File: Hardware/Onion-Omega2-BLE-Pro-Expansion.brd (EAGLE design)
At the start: 57 x 39 mm, 50 parts, among them J1 USB-MICROB, J2 USB-A-H, Q1 12Mhz 3225 Package

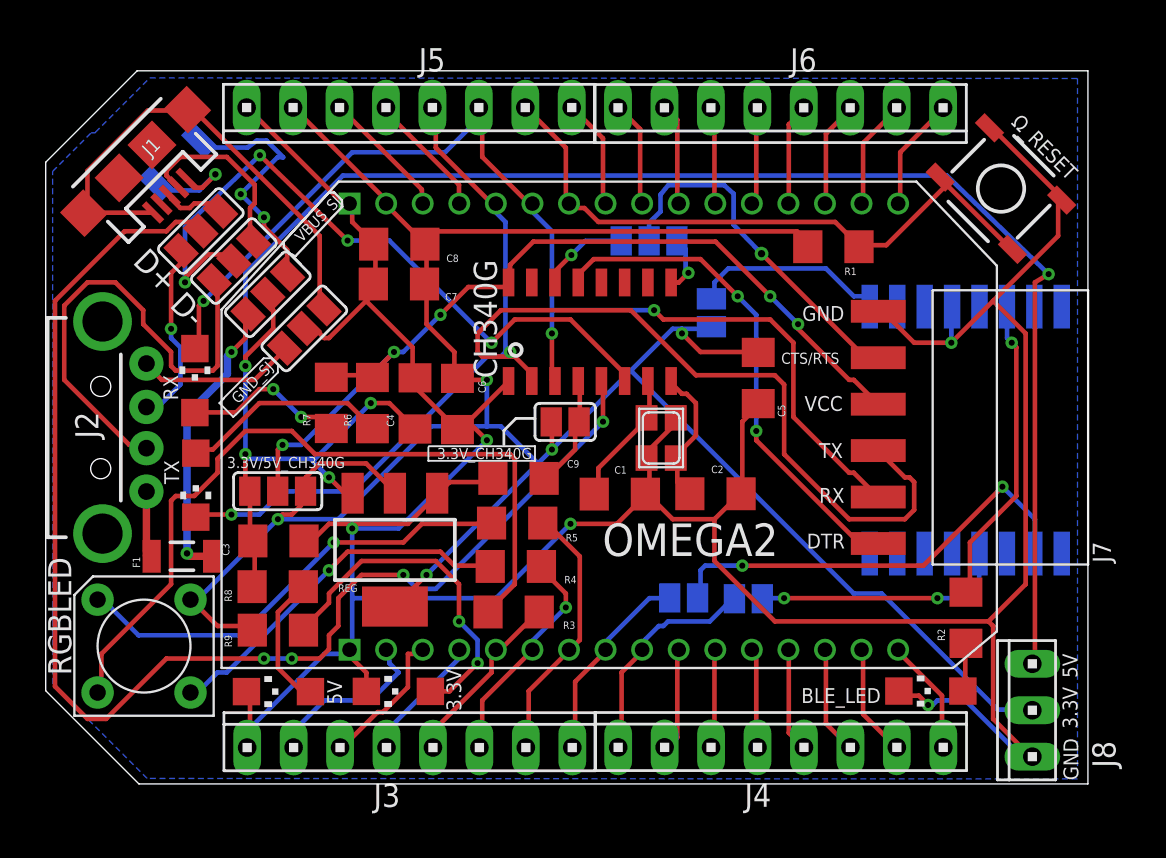
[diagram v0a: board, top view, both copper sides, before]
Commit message: VBUS fused moved after jumper. Resistors for D+ and D- Lines. TODO: Reduce D+ line length
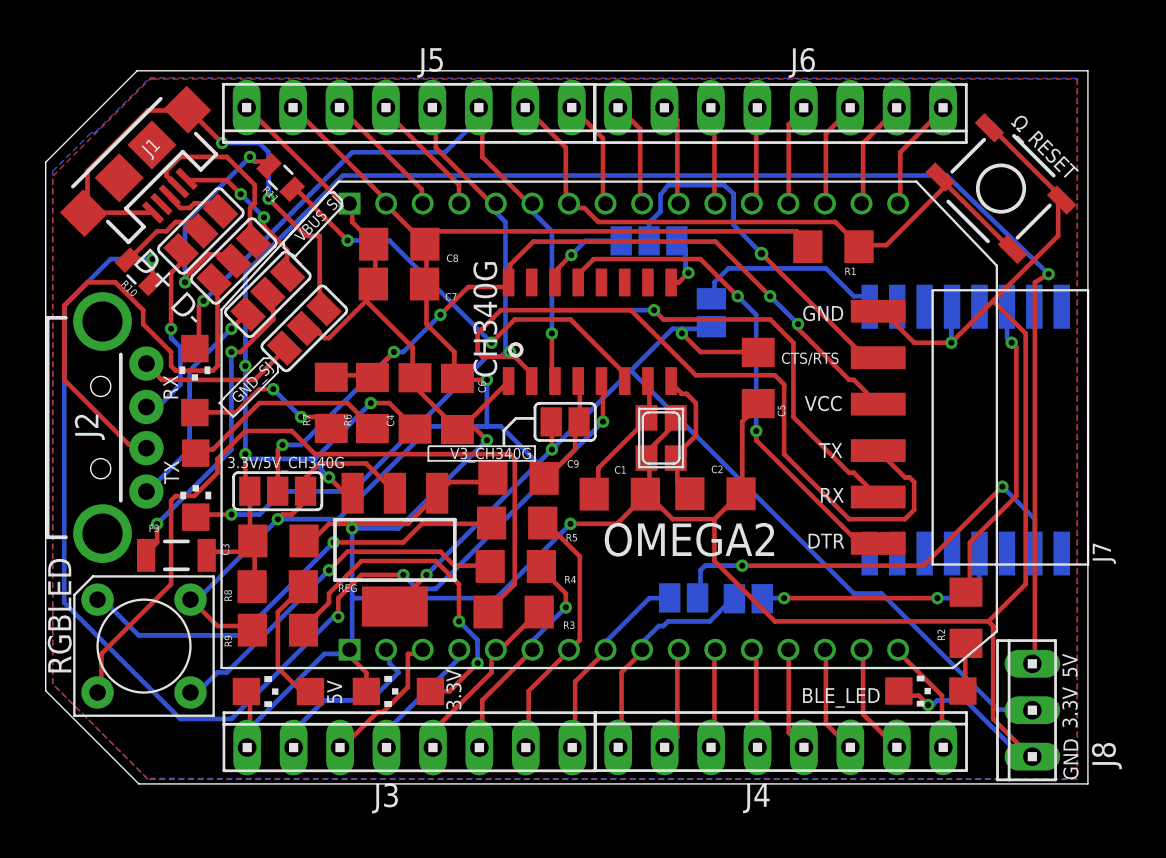
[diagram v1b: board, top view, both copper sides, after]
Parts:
- removed F1, F2: PTCSMD-W, SparkFun-PowerIC:PTC-1206-WIDE
- added F3: PTCSMD-W, SparkFun-PowerIC:PTC-1206-WIDE
- added R10, R11: (no value), SparkFun-Passives:0805
- renumbered 3.3V_CH340G to V3_CH340G
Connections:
- new net N$38: D+.2, R10.2
- net 5V: now also F3.2; no longer VBUS_SJ.2
- net D+: now also R10.1; no longer D+.2
- net D-: now also R11.1; no longer D-.2
- net N$27: now also F3.1, VBUS_SJ.2; no longer F2.1, J1.VBUS
- net N$37: now also VBUS_SJ.1; no longer F1.1
- net N$41: now also J1.VBUS; no longer F2.2
- net N$44: now also D-.2, R11.2; no longer F1.2, VBUS_SJ.1
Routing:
- net D-: track 38.7 -> 23.9 mm, vias 4 -> 2
- net N$27: track 5.83 -> 17.6 mm, vias 1 -> 2
- net N$37: track 3.95 -> 12.1 mm, vias 0 -> 1
- net D+: track 72.8 -> 65.8 mm
- net N$41: track 13.9 -> 8.74 mm
- net N$38: track 0.00 -> 5.12 mm
- net N$44: track 16.0 -> 13.3 mm
- net N$40: track 27.5 -> 28.8 mm, vias 0 -> 2
- net 5V: track 106.6 -> 105.3 mm
- added copper zone on layer 1, net 3.3V

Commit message: CTS and RTS lines seperated. Sent for production
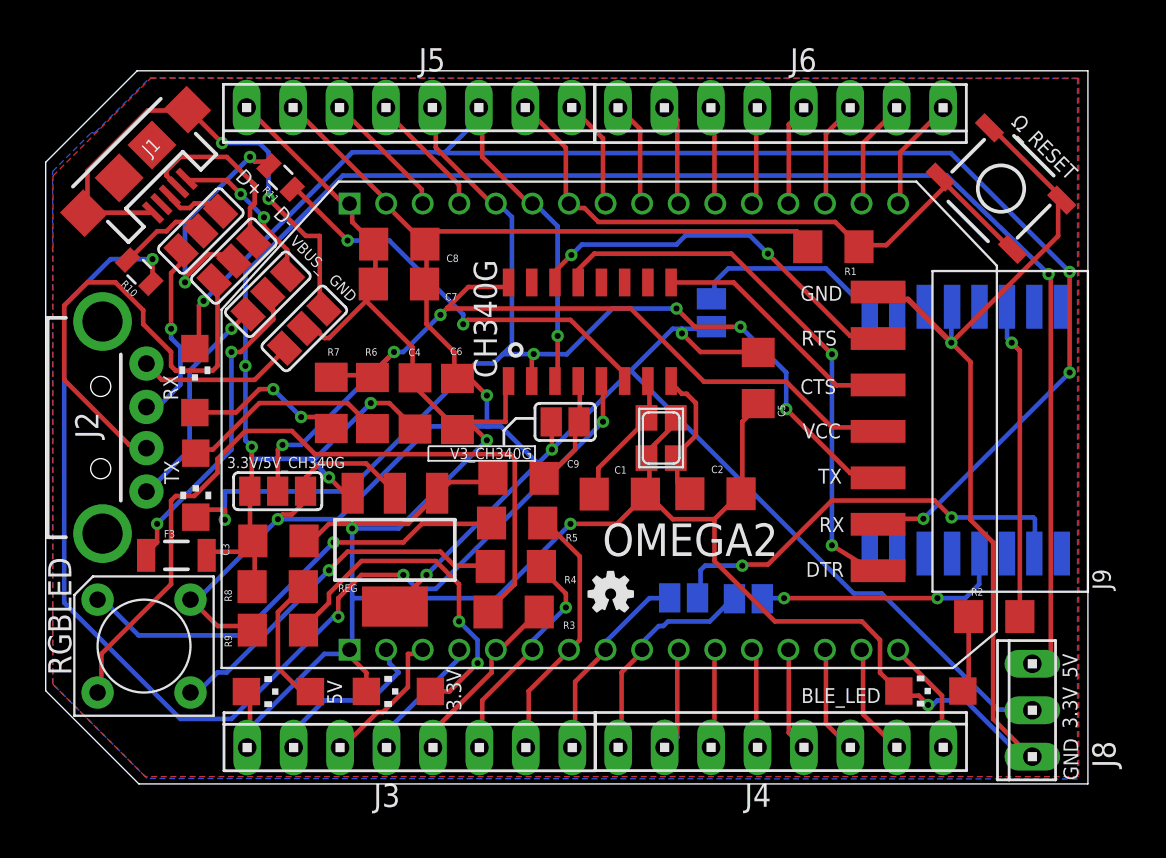
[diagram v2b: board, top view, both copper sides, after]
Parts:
- removed CTS/RTS: (no value), jumper:SJ_2
- removed J7: (no value), SparkFun-Connectors:1X06-SMD-FEMALE-V2
- added J9: (no value), SparkFun-Connectors:1X07-SMD-FEMALE-V2
- added LOGO1: OSHW-LOGOMINI, SparkFun-Aesthetics:OSHW-LOGO-MINI
- moved R2 1.55 mm to (51.9, 9.15), turned to 0 degrees
- renumbered GND_SJ to GND, VBUS_SJ to VBUS_
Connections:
- removed net N$48: CTS/RTS.2, J7.2
- net CTS: now also J9.3; no longer CTS/RTS.1
- net DTR: now also J9.7; no longer J7.6
- net GND: now also J9.1; no longer J7.1
- net RTS: now also J9.2; no longer CTS/RTS.3
- net RX_CH340: now also J9.6; no longer J7.5
- net TX_CH340: now also J9.5; no longer J7.4
- net VCC: now also J9.4; no longer J7.3
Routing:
- net RX_CH340: track 64.2 -> 96.2 mm, vias 3 -> 5
- net N$48: track 19.9 -> 0.00 mm, vias 1 -> 0
- net RTS: track 4.92 -> 21.5 mm, vias 1 -> 2
- net TX_CH340: track 77.3 -> 66.6 mm, vias 2 -> 5
- net CTS: track 3.17 -> 13.7 mm, vias 1 -> 0
- net GND: track 189.6 -> 185.9 mm
- net DTR: track 27.7 -> 30.9 mm
- net N$4: track 2.75 -> 4.28 mm
- net 5V: track 105.3 -> 106.7 mm
- net VCC: track 48.4 -> 49.3 mm, vias 5 -> 3
- net N$3: track 17.0 -> 17.6 mm
- net D-: track 23.9 -> 23.3 mm
- added copper zone on layer 16, net GND
- removed copper zone on layer 16, net N$10
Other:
- board text added: "CTS"
- board text added: "RTS"
- board text removed: "CTS/RTS"
